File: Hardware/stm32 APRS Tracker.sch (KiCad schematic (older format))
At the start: 62 parts, among them IC1 STM32F103x, P101 CONN_01X04, P102 CONN_01X05, P103 CONN_01X01, SW101 SW_TxPwr, U101 STM32_mmvisual_JTAG, Y101 8 MHz, Y102 32,768

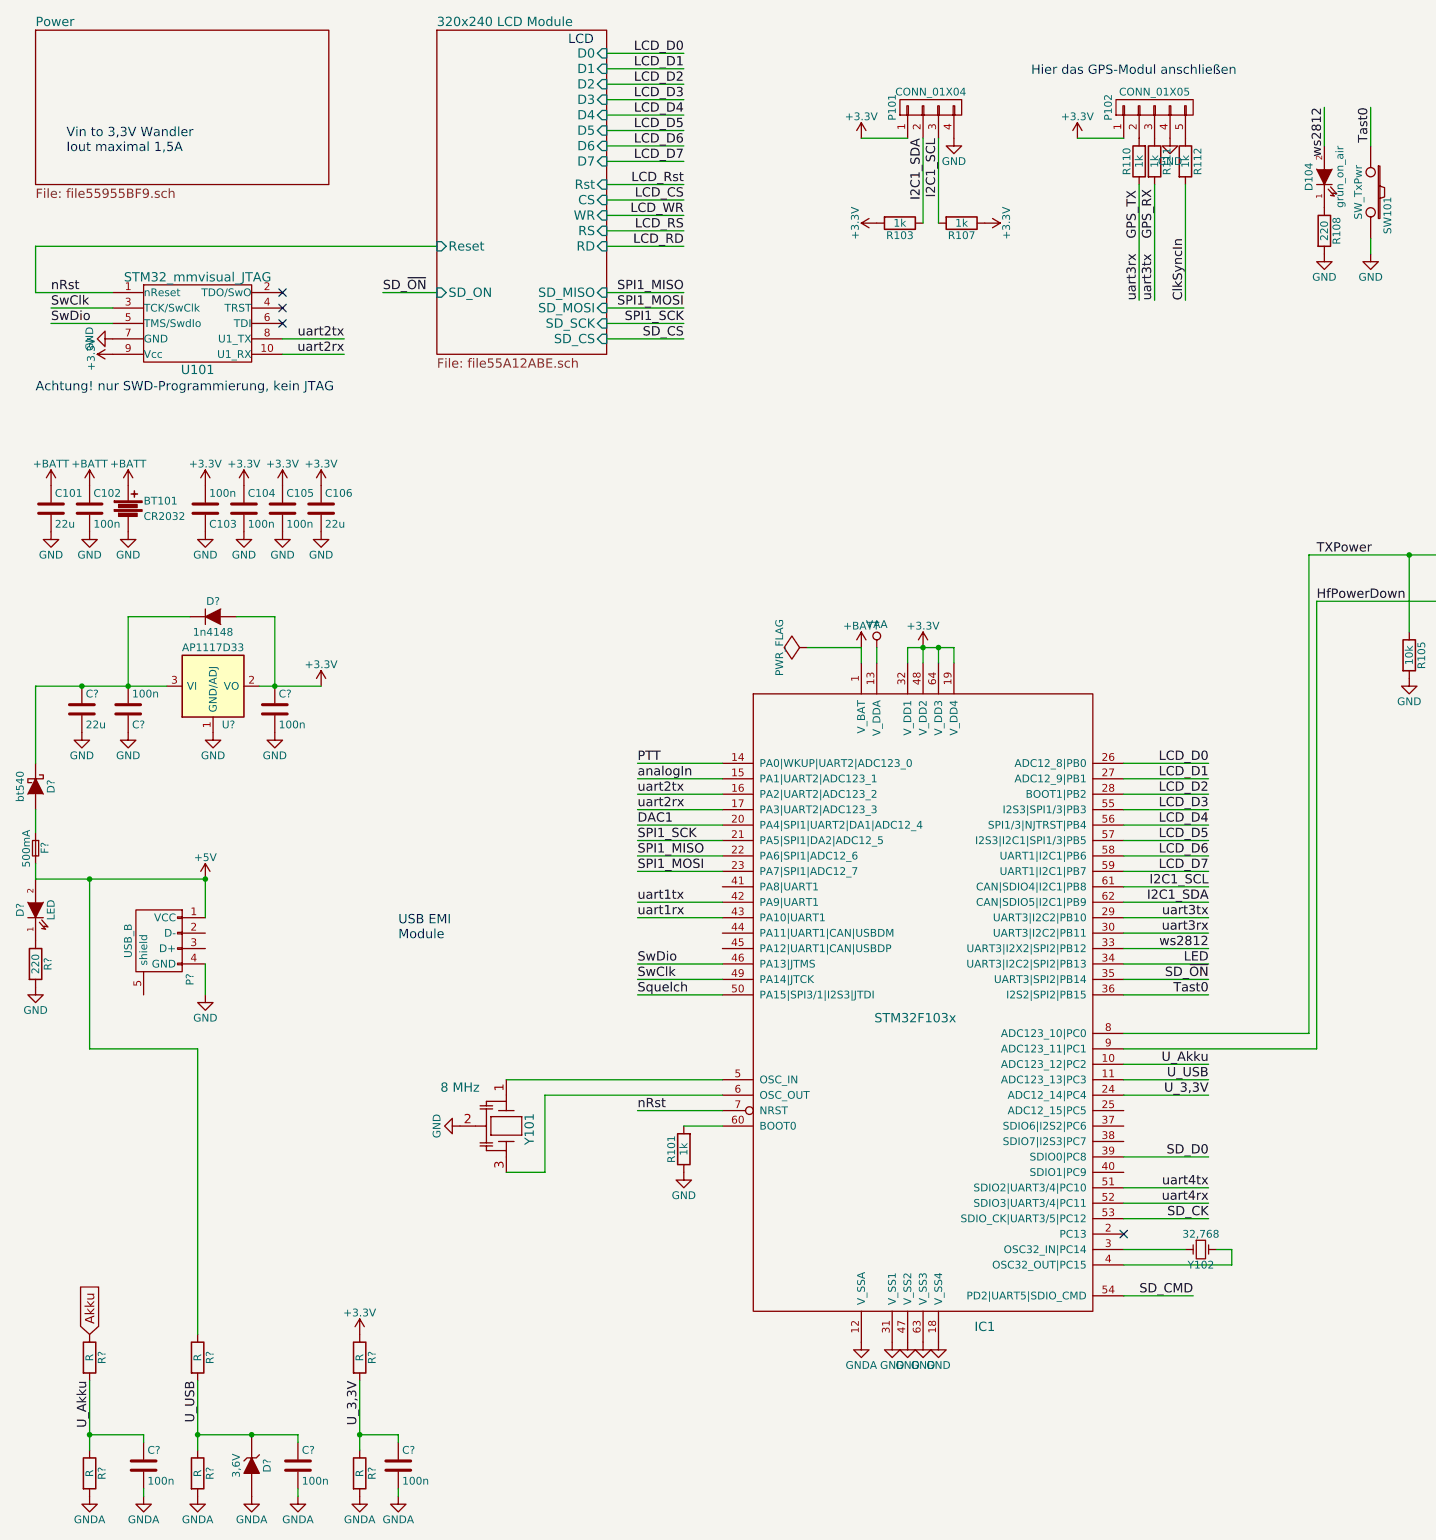
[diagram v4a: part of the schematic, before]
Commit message: neuer stm eingebunden und adcs angeschlossen
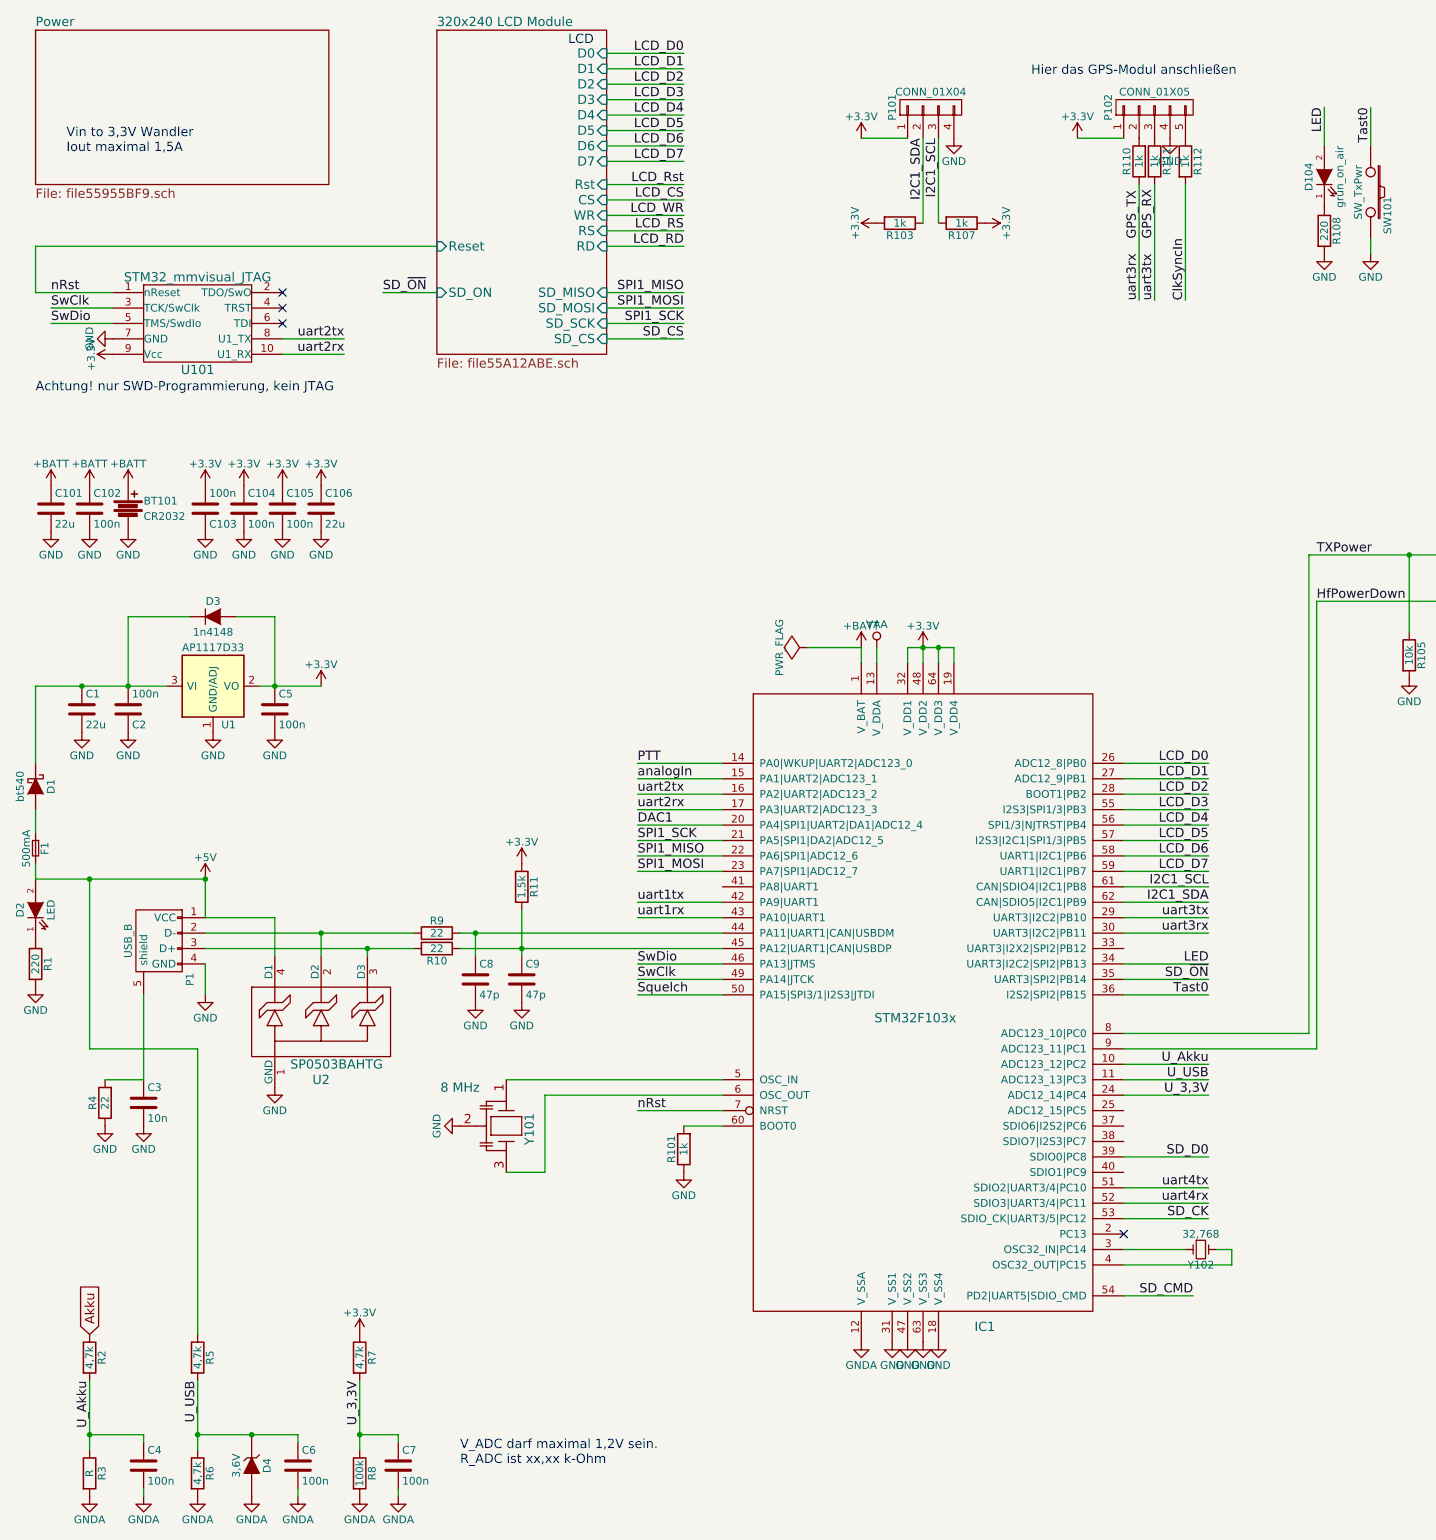
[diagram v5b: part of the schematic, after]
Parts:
- added C3: 10n, Capacitors_ThroughHole:C_Disc_D3_P2.5, symbol C
- added C8, C9: 47p, Capacitors_SMD:C_0603, symbol C
- added R10, R9: 22, symbol R
- added R11: 1,5k, symbol R
- added R4: 22, Resistors_ThroughHole:Resistor_Horizontal_RM10mm, symbol R
- added U2: SP0503BAHTG, symbol SP0503BAHTG
- R2, R5, R6, R7: renamed from R?; value R -> 4,7k
- R8: renamed from R?; value R -> 100k
- gave numbers to parts that had none: 15
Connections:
- net +3V3: now also R11.1
- net +5V: now also U2.4 (D1)
- net GND: now also C3.2, C8.2, C9.2, R4.1, U2.1 (GND)
- net LED: now also D104.2 (A)
- net at IC1.44 (PA11|UART1|CAN|USBDM): now also C8.1, R9.2
- net at IC1.45 (PA12|UART1|CAN|USBDP): now also C9.1, R10.1, R11.2
- net at P1.2 (D-): now also R9.1, U2.2 (D2)
- net at P1.3 (D+): now also R10.2, U2.3 (D3)
- net at P1.5 (shield): now also C3.1, R4.2
- net ws2812: no longer names the net of IC1.33 (UART3|I2X2|SPI2|PB12)
- net ws2812: no longer D104.2 (A)
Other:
- note added: "V_ADC darf maximal 1,2V sein.\nR_ADC ist xx,xx k-Ohm"
- note removed: "USB EMI\nModule"

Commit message: Schaltplan momentan fertig - Netzliste angefangen.
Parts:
- removed P102: CONN_01X05, symbol CONN_01X05
- removed R112: 1k, symbol R
- added D101: grün_on_air, LEDs:LED-0603, symbol LED
- added D102: orange_txprw_high, LEDs:LED-0603, symbol LED
- added D103: rot_logging_on, LEDs:LED-0603, symbol LED
- added P102: CONN_01X04, Pin_Headers:Pin_Header_Straight_1x04, symbol CONN_01X04
- added R102, R104, R106: 220, Resistors_SMD:R_0603, symbol R
- added RP101: 3,3k, Resistors_SMD:R_Array_Convex_4x0603, symbol R_PACK4
- D104: value grün_on_air -> grün_gps_lock
- D2: footprint (none) -> LEDs:LED-0603
- D3: footprint (none) -> Diodes_SMD:Diode-MiniMELF_Standard
- IC1: footprint (none) -> Housings_QFP:LQFP-64_10x10mm_Pitch0.5mm
- P101: footprint (none) -> Pin_Headers:Pin_Header_Straight_1x04
- P103: footprint (none) -> Pin_Headers:Pin_Header_Straight_1x01
- R1, R10, R103, R105, R107, R108, R11, R110, R111, R2, R3, R5, R6, R7, R8, R9: footprint (none) -> Resistors_SMD:R_0603
- U1: footprint (none) -> Housings_SOT-89:SOT89-3_Housing
- Y101: footprint (none) -> PhilippsFootprints:CSTCE_3,2x1,3
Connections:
- net uart4rx is gone; now on net LCD_RD: IC1.52 (SDIO3|UART3/4|PC11)
- net uart4tx is gone; now on net LCD_RS: IC1.51 (SDIO2|UART3/4|PC10)
- net +3V3: now also P102.1 (P1), RP101.1 (P1), RP101.2 (P2), RP101.3 (P3), RP101.4 (P4)
- net GND: now also P102.4 (P4), R102.2, R104.2, R106.2
- net LCD_CS: now also IC1.38 (SDIO7|I2S3|PC7)
- net LCD_Rst: now also IC1.41 (PA8|UART1)
- net LCD_WR: now also IC1.40 (SDIO1|PC9)
- net SD_CK: now also RP101.7 (R2)
- net SD_CMD: now also RP101.6 (R3)
- net SD_CS: now also RP101.8 (R1)
- net SD_~ON: now also IC1.25 (ADC12_15|PC5); no longer IC1.35 (UART3|SPI2|PB14)
- net Tast0: now also IC1.37 (SDIO6|I2S2|PC6); no longer IC1.36 (I2S2|SPI2|PB15)
- net at R110.2: now also P102.2 (P2)
- net at R111.1: now also P102.3 (P3)
- net LED_0: now reaches IC1.33 (UART3|I2X2|SPI2|PB12)
- net LED_0: now also D104.2 (A)
- net LED renamed LED_1
- net LED_1: now also D101.2 (A); no longer D104.2 (A)
- net SD_D0 renamed SD_Data
- net SD_Data: now also RP101.5 (R4)
- new net: D103.1 (K), R106.1
- new net: D102.1 (K), R104.1
- new net: D101.1 (K), R102.1
- new net LED_2: D102.2 (A), IC1.35 (UART3|SPI2|PB14)
- new net LED_3: D103.2 (A), IC1.36 (I2S2|SPI2|PB15)
- no-connect marks 4 -> 7
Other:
- note added: "IMU modul hier anbringen"
- moved on the sheet: SW101

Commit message: Platine angefangen - es wird auf jeden Fall eng
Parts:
- added D105: 5V TVS, symbol ZENER
- D1: value bt540 -> STPS340U; footprint (none) -> Diodes_SMD:Diode-SMB_Standard
- D4: footprint (none) -> Diodes_SMD:Diode-MiniMELF_Standard
- P1: footprint (none) -> Connect:USB_Mini-B
- U101: footprint (none) -> con-amp-micromatch:con-amp-micromatch-MICROMATCH-10
- U2: footprint (none) -> Housings_SOT-23_SOT-143_TSOT-6:SOT-143
- Y102: footprint (none) -> Capacitors_SMD:C_1206
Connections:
- net +5V: now also D105.1 (K)
- net GND: now also D105.2 (A)
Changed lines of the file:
@@
 F 0 "U101" H 2200 2600 60  0000 C CNN
 F 1 "STM32_mmvisual_JTAG" H 2200 3200 60  0000 C CNN
-F 2 "" H 1250 2600 60  0001 C CNN
+F 2 "con-amp-micromatch:con-amp-micromatch-MICROMATCH-10" H 1250 2600 60  0001 C CNN
 F 3 "" H 1250 2600 60  0000 C CNN
 	1    2200 2900
@@
 F 0 "Y102" H 8700 9000 50  0000 C CNN
 F 1 "32,768" H 8700 8800 50  0000 C CNN
-F 2 "" H 8700 8900 60  0001 C CNN
+F 2 "Capacitors_SMD:C_1206" H 8700 8900 60  0001 C CNN
 F 3 "" H 8700 8900 60  0000 C CNN
 	1    8700 8900
@@
 F 0 "P1" H 2150 6750 50  0000 C CNN
 F 1 "USB_B" H 1900 7150 50  0000 C CNN
-F 2 "" V 1900 6850 60  0001 C CNN
+F 2 "Connect:USB_Mini-B" V 1900 6850 60  0001 C CNN
 F 3 "" V 1900 6850 60  0000 C CNN
 	1    1950 6950
@@
 P 1150 5900
 F 0 "D1" H 1150 6000 50  0000 C CNN
-F 1 "bt540" H 1150 5800 50  0000 C CNN
-F 2 "" H 1150 5900 60  0001 C CNN
+F 1 "STPS340U" H 1150 5800 50  0000 C CNN
+F 2 "Diodes_SMD:Diode-SMB_Standard" H 1150 5900 60  0001 C CNN
 F 3 "" H 1150 5900 60  0000 C CNN
 	1    1150 5900
@@
 	2250 6500 2250 6750
 Wire Wire Line
-	1150 6500 2250 6500
+	850  6500 2250 6500
 Wire Wire Line
 	1150 6500 1150 6400
@@
 F 0 "D4" H 2550 10400 50  0000 C CNN
 F 1 "3,6V" H 2550 10200 50  0000 C CNN
-F 2 "" H 2550 10300 60  0001 C CNN
+F 2 "Diodes_SMD:Diode-MiniMELF_Standard" H 2550 10300 60  0001 C CNN
 F 3 "" H 2550 10300 60  0000 C CNN
 	1    2550 10300
@@
 F 0 "U2" H 3000 7100 60  0000 C CNN
 F 1 "SP0503BAHTG" H 3100 7200 60  0000 C CNN
-F 2 "" H 1900 6350 60  0001 C CNN
+F 2 "Housings_SOT-23_SOT-143_TSOT-6:SOT-143" H 1900 6350 60  0001 C CNN
 F 3 "" H 1900 6350 60  0000 C CNN
 	1    3000 7450
@@
 Text Notes 6250 1300 0    60   ~ 0
 IMU modul hier anbringen
+$Comp
+L ZENER D105
+U 1 1 55A90BD7
+P 850 6700
+F 0 "D105" H 850 6800 50  0000 C CNN
+F 1 "5V TVS" H 850 6600 50  0000 C CNN
+F 2 "" H 850 6700 60  0001 C CNN
+F 3 "" H 850 6700 60  0000 C CNN
+	1    850  6700
+	0    1    1    0
+$EndComp
+$Comp
+L GND #PWR080
+U 1 1 55A90EB5
+P 850 6900
+F 0 "#PWR080" H 850 6650 50  0001 C CNN
+F 1 "GND" H 850 6750 50  0000 C CNN
+F 2 "" H 850 6900 60  0000 C CNN
+F 3 "" H 850 6900 60  0000 C CNN
+	1    850  6900
+	1    0    0    -1
+$EndComp
+Connection ~ 1150 6500
 $EndSCHEMATC

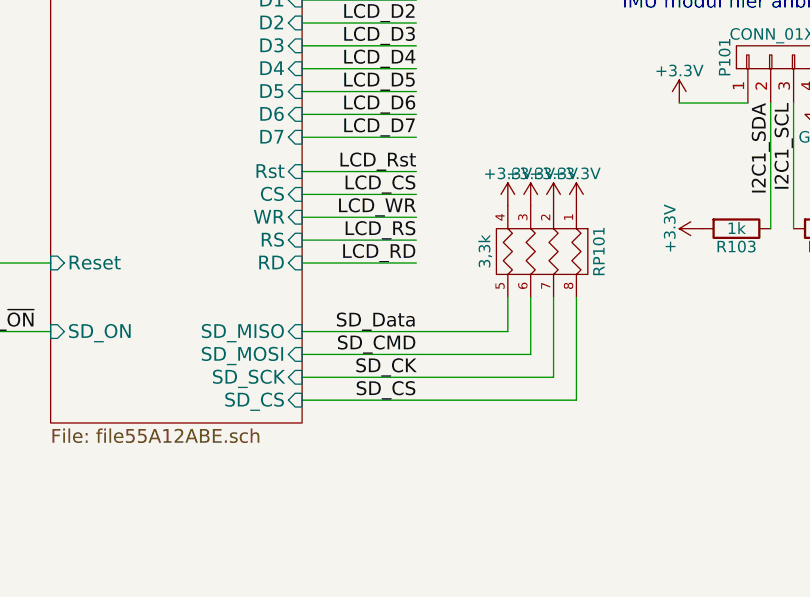
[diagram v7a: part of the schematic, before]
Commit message: Layout durchaus weiter, STM fast komplett angeschlossen
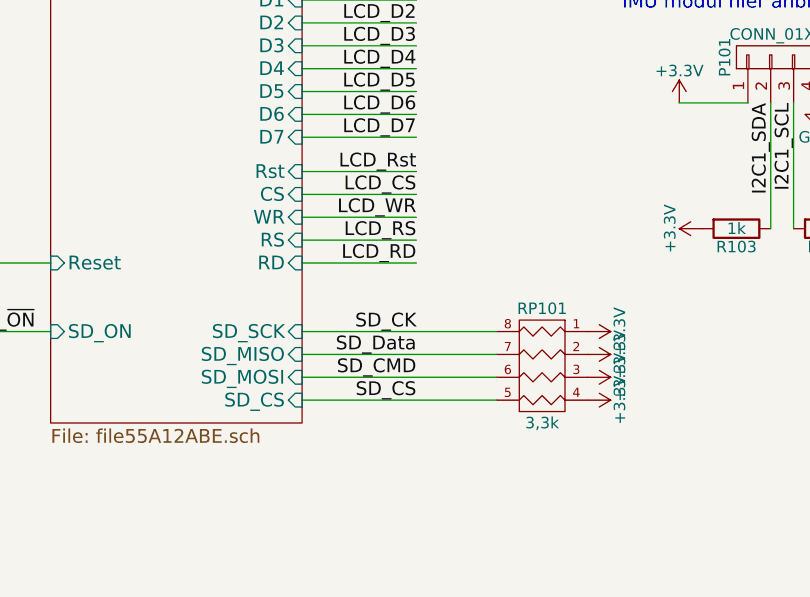
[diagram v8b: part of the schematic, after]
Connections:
- net SD_CK: now also RP101.8 (R1); no longer RP101.7 (R2)
- net SD_CS: now also RP101.5 (R4); no longer RP101.8 (R1)
- net SD_Data: now also RP101.7 (R2); no longer RP101.5 (R4)
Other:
- moved on the sheet: RP101
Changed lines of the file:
@@
 F13 "RS" I R 4850 2300 60
 F14 "RD" I R 4850 2400 60
-F15 "SD_MISO" I R 4850 2700 60
-F16 "SD_MOSI" I R 4850 2800 60
-F17 "SD_SCK" I R 4850 2900 60
+F15 "SD_MISO" I R 4850 2800 60
+F16 "SD_MOSI" I R 4850 2900 60
+F17 "SD_SCK" I R 4850 2700 60
 F18 "SD_CS" I R 4850 3000 60
 F19 "SD_ON" I L 3750 2700 60
@@
 Text Label 5350 3000 2    60   ~ 0
 SD_CS
-Wire Wire Line
-	4850 2700 5750 2700
-Wire Wire Line
-	4850 2800 5850 2800
-Wire Wire Line
-	4850 2900 5950 2900
-Wire Wire Line
-	4850 3000 6050 3000
 Text Label 10900 1500 3    60   ~ 0
 Tast0
@@
 	0    -1   -1   0
 $EndComp
+Text Label 5350 2700 2    60   ~ 0
+SD_CK
 Text Label 5350 2900 2    60   ~ 0
-SD_CK
+SD_CMD
 Text Label 5350 2800 2    60   ~ 0
-SD_CMD
-Text Label 5350 2700 2    60   ~ 0
 SD_Data
 $Comp
 L R_PACK4 RP101
 U 1 1 55A559BC
-P 5700 2350
-F 0 "RP101" H 5700 2800 50  0000 C CNN
-F 1 "3,3k" H 5700 2300 50  0000 C CNN
-F 2 "Resistors_SMD:R_Array_Convex_4x0603" H 5700 2350 60  0001 C CNN
-F 3 "" H 5700 2350 60  0000 C CNN
-	1    5700 2350
-	0    1    1    0
+P 5900 3050
+F 0 "RP101" H 5900 3500 50  0000 C CNN
+F 1 "3,3k" H 5900 3000 50  0000 C CNN
+F 2 "Resistors_SMD:R_Array_Convex_4x0603" H 5900 3050 60  0001 C CNN
+F 3 "" H 5900 3050 60  0000 C CNN
+	1    5900 3050
+	-1   0    0    -1
 $EndComp
 $Comp
 L +3.3V #PWR075
 U 1 1 55A55B69
-P 5750 2150
-F 0 "#PWR075" H 5750 2000 50  0001 C CNN
-F 1 "+3.3V" H 5750 2290 50  0000 C CNN
-F 2 "" H 5750 2150 60  0000 C CNN
-F 3 "" H 5750 2150 60  0000 C CNN
-	1    5750 2150
-	1    0    0    -1
+P 6100 3000
+F 0 "#PWR075" H 6100 2850 50  0001 C CNN
+F 1 "+3.3V" H 6100 3140 50  0000 C CNN
+F 2 "" H 6100 3000 60  0000 C CNN
+F 3 "" H 6100 3000 60  0000 C CNN
+	1    6100 3000
+	0    1    -1   0
 $EndComp
 $Comp
 L +3.3V #PWR076
 U 1 1 55A55CCA
-P 5850 2150
-F 0 "#PWR076" H 5850 2000 50  0001 C CNN
-F 1 "+3.3V" H 5850 2290 50  0000 C CNN
-F 2 "" H 5850 2150 60  0000 C CNN
-F 3 "" H 5850 2150 60  0000 C CNN
-	1    5850 2150
-	1    0    0    -1
+P 6100 2900
+F 0 "#PWR076" H 6100 2750 50  0001 C CNN
+F 1 "+3.3V" H 6100 3040 50  0000 C CNN
+F 2 "" H 6100 2900 60  0000 C CNN
+F 3 "" H 6100 2900 60  0000 C CNN
+	1    6100 2900
+	0    1    -1   0
 $EndComp
 $Comp
 L +3.3V #PWR077
 U 1 1 55A55E2B
-P 5950 2150
-F 0 "#PWR077" H 5950 2000 50  0001 C CNN
-F 1 "+3.3V" H 5950 2290 50  0000 C CNN
-F 2 "" H 5950 2150 60  0000 C CNN
-F 3 "" H 5950 2150 60  0000 C CNN
-	1    5950 2150
-	1    0    0    -1
-$EndComp
-Wire Wire Line
-	5750 2700 5750 2550
-Wire Wire Line
-	5850 2800 5850 2550
-Wire Wire Line
-	5950 2900 5950 2550
+P 6100 2800
+F 0 "#PWR077" H 6100 2650 50  0001 C CNN
+F 1 "+3.3V" H 6100 2940 50  0000 C CNN
+F 2 "" H 6100 2800 60  0000 C CNN
+F 3 "" H 6100 2800 60  0000 C CNN
+	1    6100 2800
+	0    1    -1   0
+$EndComp
 $Comp
 L +3.3V #PWR078
 U 1 1 55A56462
-P 6050 2150
-F 0 "#PWR078" H 6050 2000 50  0001 C CNN
-F 1 "+3.3V" H 6050 2290 50  0000 C CNN
-F 2 "" H 6050 2150 60  0000 C CNN
-F 3 "" H 6050 2150 60  0000 C CNN
-	1    6050 2150
-	1    0    0    -1
-$EndComp
-Wire Wire Line
-	6050 3000 6050 2550
+P 6100 2700
+F 0 "#PWR078" H 6100 2550 50  0001 C CNN
+F 1 "+3.3V" H 6100 2840 50  0000 C CNN
+F 2 "" H 6100 2700 60  0000 C CNN
+F 3 "" H 6100 2700 60  0000 C CNN
+	1    6100 2700
+	0    1    -1   0
+$EndComp
 NoConn ~ 5600 6250
 NoConn ~ 5600 6350
@@
 $EndComp
 Connection ~ 1150 6500
+Wire Wire Line
+	4850 2800 5700 2800
+Wire Wire Line
+	4850 2900 5700 2900
+Wire Wire Line
+	4850 2700 5700 2700
+Wire Wire Line
+	4850 3000 5700 3000
 $EndSCHEMATC
